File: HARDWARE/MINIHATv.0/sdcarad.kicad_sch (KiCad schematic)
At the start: 14 parts, among them J2 Micro_SD_Card_Det2

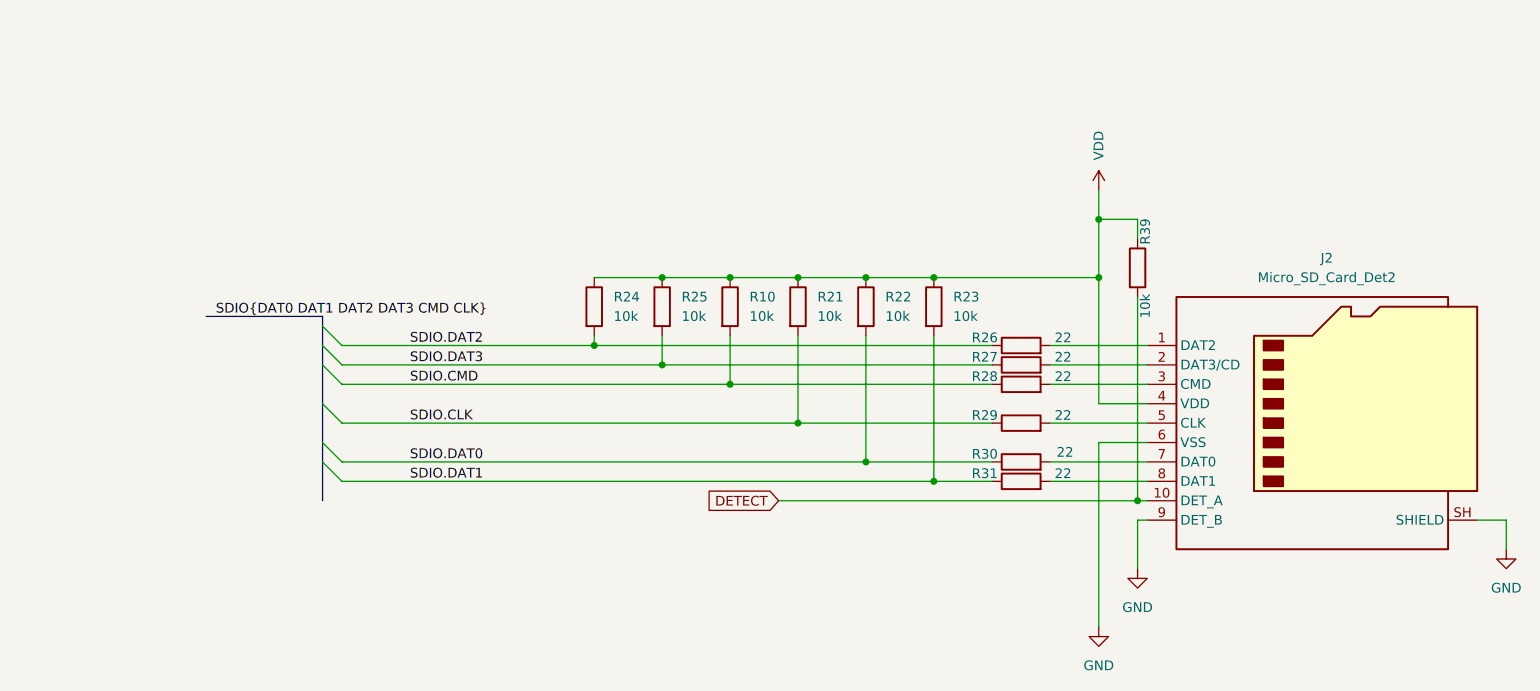
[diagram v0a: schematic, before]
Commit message: added normal buses
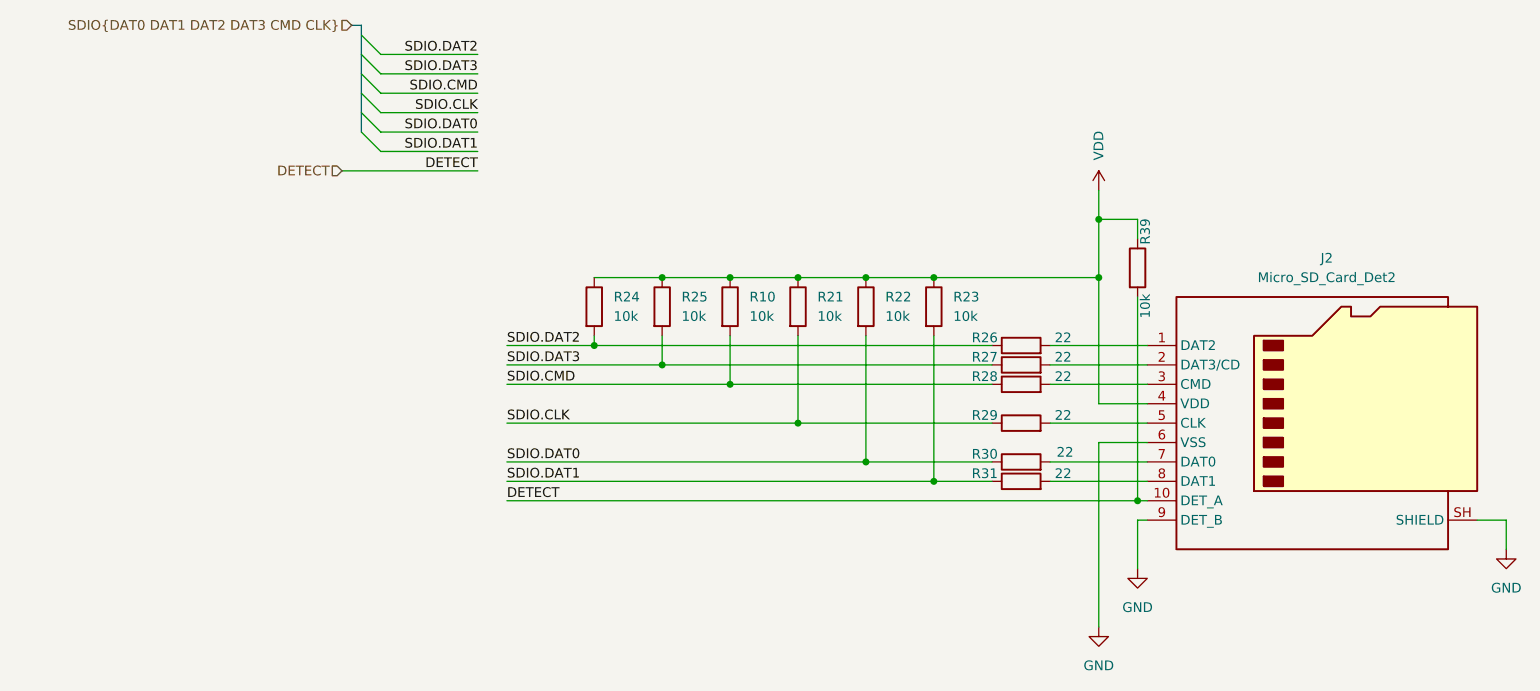
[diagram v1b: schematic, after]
